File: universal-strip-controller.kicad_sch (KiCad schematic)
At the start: 50 parts, among them J1 Conn_01x03_Pin, J2 Conn_01x02_Pin, SW1 434133025816, SW2 434133025816, U1 RP2350B, U2 RPI RM2, U3 W25Q128JVSIQ, U9 DS3231SN, X1 12MHz

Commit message: Added power sensing for each of the VIN zones
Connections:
- net STRING0: no longer R9.1
- net GPIO33: no longer names the net of U1.42 (GPIO33)
- net GPIO34: no longer names the net of U1.43 (GPIO34)
- net GPIO35: no longer names the net of U1.44 (GPIO35)
- net GPIO45_ADC5: no longer names the net of U1.56 (GPIO45_ADC5)
- net GPIO46_ADC6: no longer names the net of U1.57 (GPIO46_ADC6)
- net GPIO47_ADC7: no longer names the net of U1.58 (GPIO47_ADC7)
- net RTC_SCL renamed MCU_SCL
- net RTC_SDA renamed MCU_SDA
- new net GPIO0: R9.1
- no-connect marks 7 -> 15

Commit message: Added RM2 footprint, about to add the others
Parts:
- U2: footprint (none) -> RF_Module:RMC20452T
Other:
- title: (none) -> Universal Strip Controller
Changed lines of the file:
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@@
 	(generator_version "10.0")
 	(paper "A3")
+	(title_block
+		(title "Universal Strip Controller")
+		(date "2026-09-10")
+		(rev "1.0")
+	)
 	(text "Make sure R7 and R8 are close to RP2350\n"
 		(exclude_from_sim no)
@@
 			)
 		)
-		(property "Footprint" ""
+		(property "Footprint" "RF_Module:RMC20452T"
 			(at 353.06 209.55 0)
 			(hide yes)

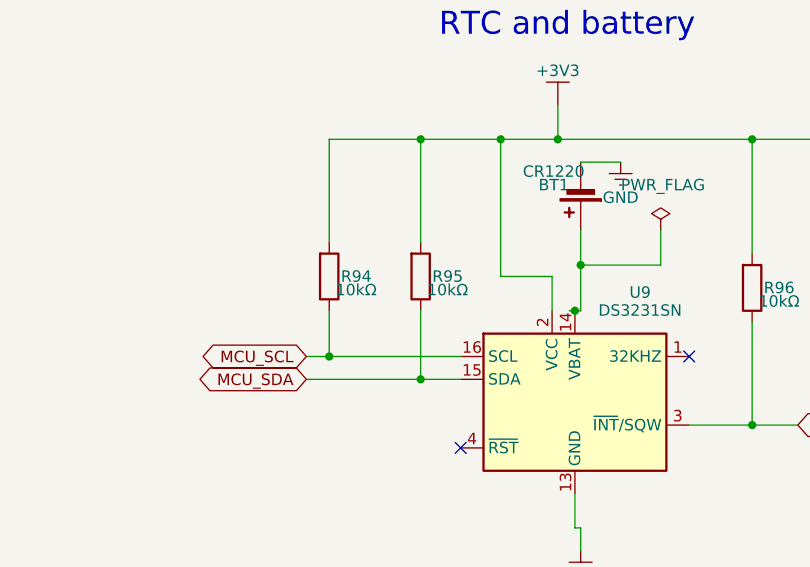
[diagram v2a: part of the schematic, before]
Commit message: Added footprints for resistors
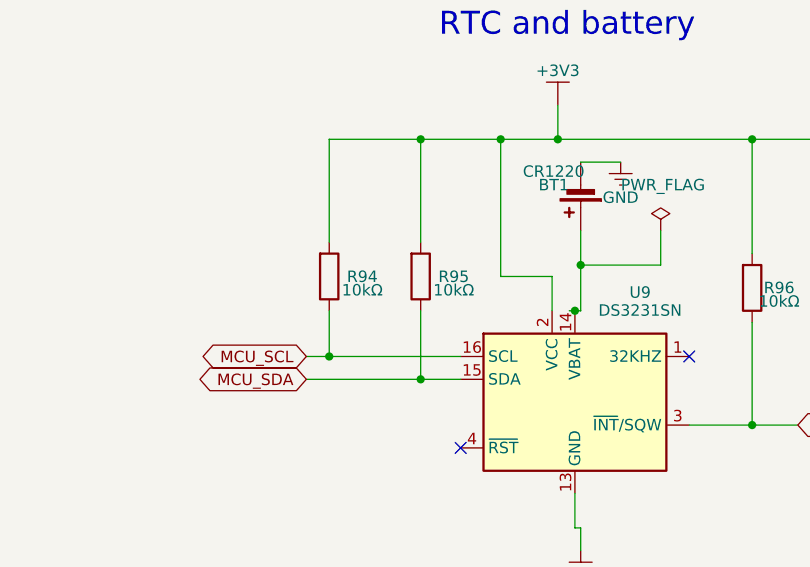
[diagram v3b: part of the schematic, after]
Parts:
- C10, C11, C12, C13, C14, C15, C16, C17, C18, C19, C2, C20, C21, C8: Manufacturer (none) -> Murata; Tolerance (none) -> 10%; manufacturer Murata -> (none); tolerance 10% -> (none)
- C3, C4: Manufacturer (none) -> Murata; Tolerance (none) -> 5%; manufacturer Murata -> (none); tolerance 5% -> (none)
- C6, C7, C9: Manufacturer (none) -> Murata; Tolerance (none) -> 20%; manufacturer Murata -> (none); tolerance 20% -> (none)
- L1: Manufacturer (none) -> Abracon; Tolerance (none) -> 20%; manufacturer Abracon -> (none); tolerance 20% -> (none)
- R1: Manufacturer (none) -> Yageo; Resistance (none) -> 10k; Tolerance (none) -> 1%; manufacturer Yageo -> (none); resistance 10k -> (none); tolerance 1% -> (none)
- R10, R9: Manufacturer (none) -> Yageo; Resistance (none) -> 0; Tolerance (none) -> +50mR; manufacturer Yageo -> (none); resistance 0 -> (none); tolerance +50mR -> (none)
- R2, R4, R6: Manufacturer (none) -> Yageo; Resistance (none) -> 1k; Tolerance (none) -> 1%; manufacturer Yageo -> (none); resistance 1k -> (none); tolerance 1% -> (none)
- R3: Manufacturer (none) -> Yageo; Resistance (none) -> 33; Tolerance (none) -> 1%; manufacturer Yageo -> (none); resistance 33 -> (none); tolerance 1% -> (none)
- R7, R8: Manufacturer (none) -> Yageo; Resistance (none) -> 27; Tolerance (none) -> 1%; manufacturer Yageo -> (none); resistance 27 -> (none); tolerance 1% -> (none)
- SW1, SW2: Manufacturer (none) -> Wurth Elektronik; manufacturer Wurth Elektronik -> (none)
- U1: Manufacturer (none) -> Raspberry Pi; manufacturer Raspberry Pi -> (none)
- U3: Manufacturer (none) -> Winbond; manufacturer Winbond -> (none)
- X1: Manufacturer (none) -> Abracon; Tolerance (none) -> 30ppm; manufacturer Abracon -> (none); tolerance 30ppm -> (none)
